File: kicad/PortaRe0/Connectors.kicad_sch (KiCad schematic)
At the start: 13 parts, among them J6 Fan, Q1 BSS138

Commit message: Docs: session34終了処理・0402化確定・ディスプレイ調査・PCBレイアウト進行中
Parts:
- R52, R53, R55, R56, R57, R60: footprint Resistor_SMD:R_0603_1608Metric -> Resistor_SMD:R_0402_1005Metric
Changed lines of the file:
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@@
 			)
 		)
-		(property "Footprint" "Resistor_SMD:R_0603_1608Metric"
+		(property "Footprint" "Resistor_SMD:R_0402_1005Metric"
 			(at 87.63 195.58 0)
 			(effects
@@
 			)
 		)
-		(property "Footprint" "Resistor_SMD:R_0603_1608Metric"
+		(property "Footprint" "Resistor_SMD:R_0402_1005Metric"
 			(at 187.96 137.16 0)
 			(effects
@@
 			)
 		)
-		(property "Footprint" "Resistor_SMD:R_0603_1608Metric"
+		(property "Footprint" "Resistor_SMD:R_0402_1005Metric"
 			(at 191.77 140.97 0)
 			(effects
@@
 			)
 		)
-		(property "Footprint" "Resistor_SMD:R_0603_1608Metric"
+		(property "Footprint" "Resistor_SMD:R_0402_1005Metric"
 			(at 102.87 198.12 0)
 			(effects
@@
 			)
 		)
-		(property "Footprint" "Resistor_SMD:R_0603_1608Metric"
+		(property "Footprint" "Resistor_SMD:R_0402_1005Metric"
 			(at 92.71 143.51 0)
 			(effects
@@
 			)
 		)
-		(property "Footprint" "Resistor_SMD:R_0603_1608Metric"
+		(property "Footprint" "Resistor_SMD:R_0402_1005Metric"
 			(at 92.71 140.97 0)
 			(effects

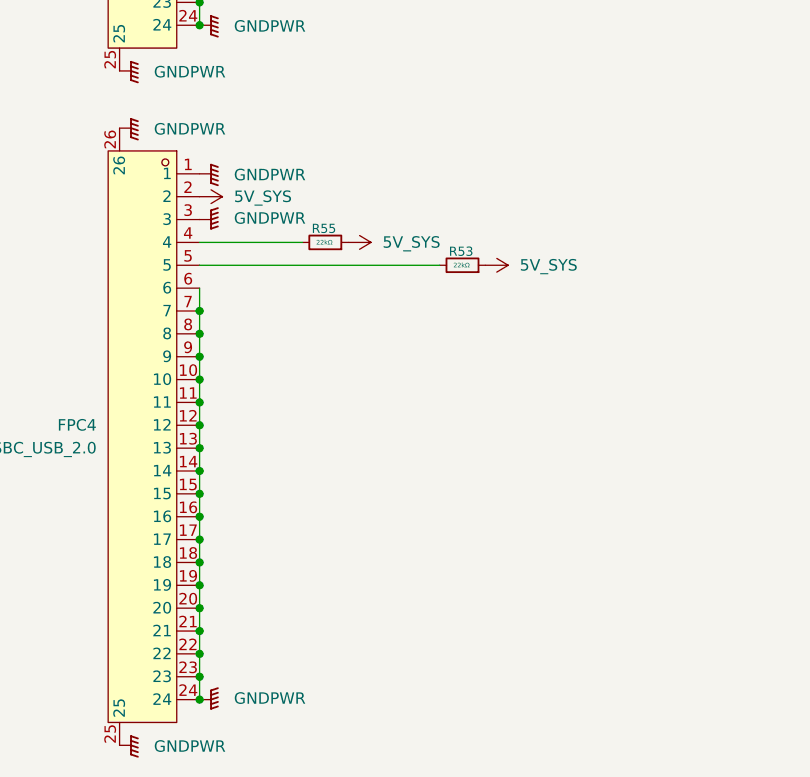
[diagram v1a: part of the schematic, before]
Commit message: Docs: session37終了処理・部品配置完了・ルーティング開始・FPC給電ピン修正
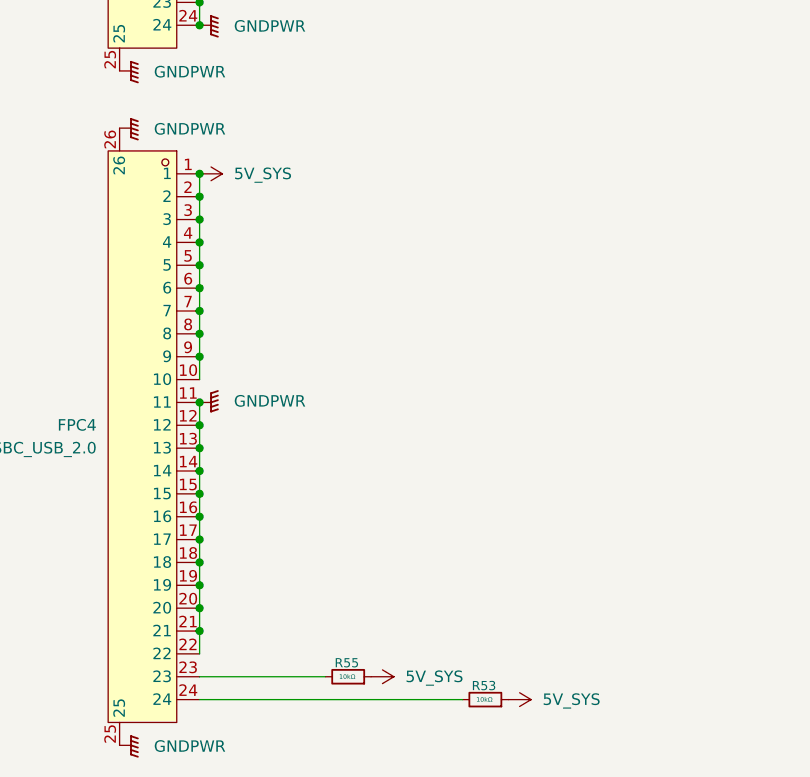
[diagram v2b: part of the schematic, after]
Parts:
- R53, R55: value 22kΩ -> 10kΩ
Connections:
- net 5V_SYS: now also FPC4.1, FPC4.10, FPC4.3, FPC4.4, FPC4.5, FPC4.6, FPC4.7, FPC4.8, FPC4.9
- net GNDPWR: no longer FPC4.1, FPC4.10, FPC4.23, FPC4.24, FPC4.3, FPC4.6, FPC4.7, FPC4.8, FPC4.9
- net at R55.2: now also FPC4.23; no longer FPC4.4
- net at R53.2: now also FPC4.24; no longer FPC4.5
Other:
- moved on the sheet: R53, R55

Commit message: Docs: session38終了処理・ルーティング大幅進捗（電源幹線〜USB差動ペア完了）
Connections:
- net 5V_SYS: no longer FPC2.18
- no-connect marks 0 -> 1
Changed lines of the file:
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@@
 		(color 0 0 0 0)
 	)
+	(no_connect
+		(at 147.32 68.58)
+	)
 	(wire
 		(pts
@@
 		(pts
 			(xy 73.66 238.76) (xy 73.66 241.3)
-		)
-		(stroke
-			(width 0)
-			(type default)
-		)
-	)
-	(wire
-		(pts
-			(xy 157.48 68.58) (xy 147.32 68.58)
 		)
 		(stroke
@@
 					(unit 1)
 				)
-			)
-		)
-	)
-	(symbol
-		(lib_id "power:5V_SYS")
-		(at 157.48 68.58 270)
-		(unit 1)
-		(exclude_from_sim no)
-		(in_bom yes)
-		(on_board yes)
-		(dnp no)
-		(fields_autoplaced yes)
-		(property "Reference" "#PWR0234"
-			(at 153.67 68.58 0)
-			(effects
-				(font
-					(size 1.27 1.27)
-				)
-				(hide yes)
-			)
-		)
-		(property "Value" "5V_SYS"
-			(at 161.29 68.5799 90)
-			(effects
-				(font
-					(size 1.27 1.27)
-				)
-				(justify left)
-			)
-		)
-		(property "Footprint" ""
-			(at 157.48 68.58 0)
-			(effects
-				(font
-					(size 1.27 1.27)
-				)
-				(hide yes)
-			)
-		)
-		(property "Datasheet" ""
-			(at 157.48 68.58 0)
-			(effects
-				(font
-					(size 1.27 1.27)
-				)
-				(hide yes)
-			)
-		)
-		(property "Description" "Power symbol creates a global label with name \"VSYS\""
-			(at 163.576 68.326 0)
-			(effects
-				(font
-					(size 1.27 1.27)
-				)
-				(hide yes)
-			)
-		)
-		(pin "1"
-		)
-		(instances
-			(project "PortaRe0"
-				(path "/479aadc4-f9a0-4ec2-b000-6a17237038f1/5dfd9f94-b7e1-4763-8093-33f7cf406206"
-					(reference "#PWR0234")
-					(unit 1)
-				)
